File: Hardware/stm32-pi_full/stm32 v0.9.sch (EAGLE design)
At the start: 271 parts, among them J1 SOLDERJUMPERNO, Q1 MMBT3906, Q2 MMBT3904, Q3 MMBT3904, U1 ESP32-WROOM-32D, Y1 6MM_3.5MM_CRYSTAL

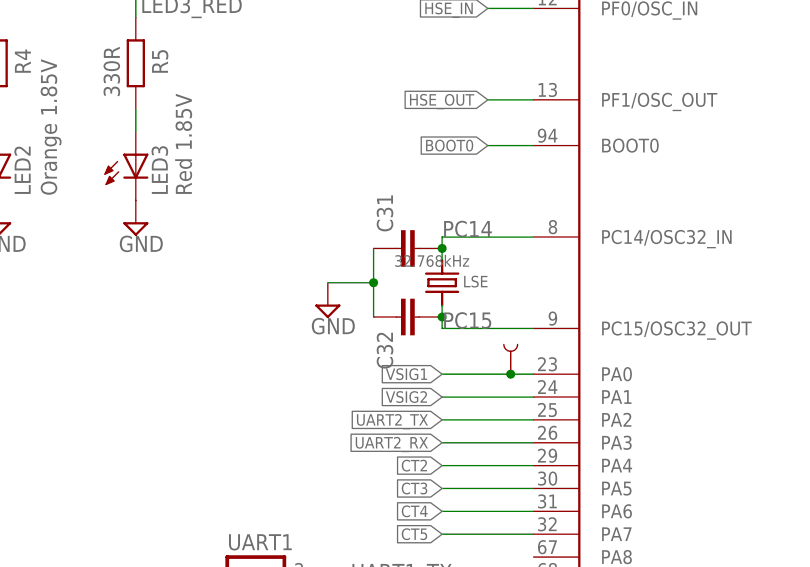
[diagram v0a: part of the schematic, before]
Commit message: non-Blocking UART transmissions
Saving 40ms at 460800 baud or 160ms at 115200 baud.
Now takes less than a millisecond to begin the UART transmit, happens in the background.
notes included on how to fire UART transmissions consequtively withing messing up the buffer or dropping transmissions.
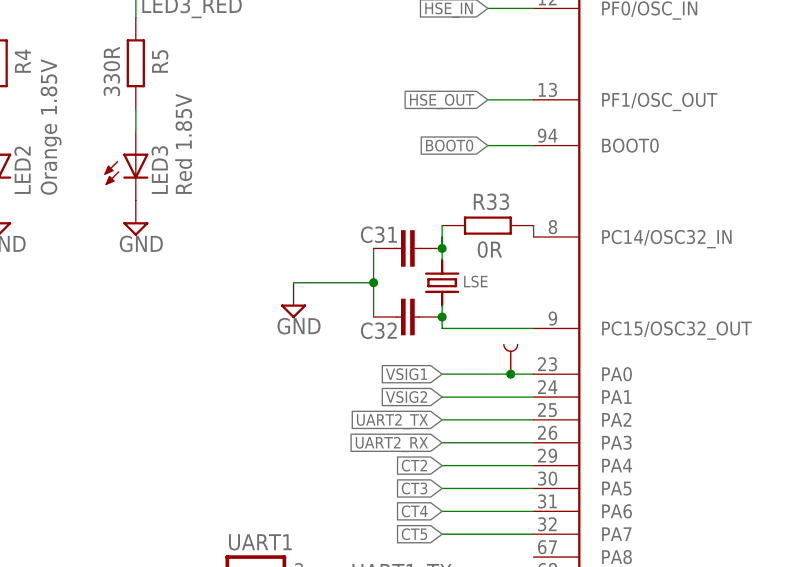
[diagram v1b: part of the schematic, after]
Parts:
- added R33: 0R, rcl:R-EU_R0603
- C29, C30: value 4.7nF -> 15pF
- C31, C32: value 2.2uF -> 10pF
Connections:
- new net N$1: R33.2, STM32F303VE.PC14/OSC32_IN
- net PC14: now also R33.1; no longer STM32F303VE.PC14/OSC32_IN
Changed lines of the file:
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@@
 <part name="R21" library="resistor" deviceset="R-EU_" device="R0603" value="0R"/>
 <part name="C21" library="rcl" library_urn="urn:adsk.eagle:library:334" deviceset="C-EU" device="C0805" package3d_urn="urn:adsk.eagle:package:23617/2" value="47uF"/>
-<part name="C29" library="rcl" library_urn="urn:adsk.eagle:library:334" deviceset="C-EU" device="C0603" package3d_urn="urn:adsk.eagle:package:23616/2" value="4.7nF"/>
-<part name="C30" library="rcl" library_urn="urn:adsk.eagle:library:334" deviceset="C-EU" device="C0603" package3d_urn="urn:adsk.eagle:package:23616/2" value="4.7nF"/>
+<part name="C29" library="rcl" library_urn="urn:adsk.eagle:library:334" deviceset="C-EU" device="C0603" package3d_urn="urn:adsk.eagle:package:23616/2" value="15pF"/>
+<part name="C30" library="rcl" library_urn="urn:adsk.eagle:library:334" deviceset="C-EU" device="C0603" package3d_urn="urn:adsk.eagle:package:23616/2" value="15pF"/>
 <part name="SUPPLY11" library="supply2" library_urn="urn:adsk.eagle:library:372" deviceset="GND" device=""/>
-<part name="C31" library="rcl" library_urn="urn:adsk.eagle:library:334" deviceset="C-EU" device="C0805" package3d_urn="urn:adsk.eagle:package:23617/2" value="2.2uF"/>
-<part name="C32" library="rcl" library_urn="urn:adsk.eagle:library:334" deviceset="C-EU" device="C0805" package3d_urn="urn:adsk.eagle:package:23617/2" value="2.2uF"/>
+<part name="C31" library="rcl" library_urn="urn:adsk.eagle:library:334" deviceset="C-EU" device="C0805" package3d_urn="urn:adsk.eagle:package:23617/2" value="10pF"/>
+<part name="C32" library="rcl" library_urn="urn:adsk.eagle:library:334" deviceset="C-EU" device="C0805" package3d_urn="urn:adsk.eagle:package:23617/2" value="10pF"/>
 <part name="SUPPLY27" library="supply2" library_urn="urn:adsk.eagle:library:372" deviceset="GND" device=""/>
 <part name="JP1" library="SparkFun-Jumpers" library_urn="urn:adsk.eagle:library:528" deviceset="JUMPER-SMT_3_1-NC_TRACE" device="_NO-SILK" package3d_urn="urn:adsk.eagle:package:39287/1"/>
@@
 <part name="R31" library="resistor" deviceset="R-EU_" device="R0603" value="0R"/>
 <part name="R32" library="resistor" deviceset="R-EU_" device="R0603" value="0R"/>
+<part name="R33" library="rcl" library_urn="urn:adsk.eagle:library:334" deviceset="R-EU_" device="R0603" package3d_urn="urn:adsk.eagle:package:23555/3" value="0R"/>
 </parts>
 <sheets>
@@
 <instance part="LSE" gate="G$1" x="53.34" y="15.24" smashed="yes" rot="R270">
 <attribute name="NAME" x="55.626" y="14.732" size="1.27" layer="95"/>
-<attribute name="VALUE" x="48.006" y="17.018" size="1.27" layer="96"/>
 </instance>
 <instance part="SUPPLY19" gate="GND" x="132.207" y="-206.629" smashed="yes">
@@
 </instance>
 <instance part="C31" gate="G$1" x="50.8" y="19.05" smashed="yes" rot="R270">
-<attribute name="NAME" x="46.101" y="25.146" size="1.778" layer="95" rot="R270"/>
+<attribute name="NAME" x="48.514" y="21.463" size="1.778" layer="95" rot="R180"/>
 </instance>
 <instance part="C32" gate="G$1" x="50.8" y="11.43" smashed="yes" rot="R270">
-<attribute name="NAME" x="46.101" y="9.906" size="1.778" layer="95" rot="R270"/>
+<attribute name="NAME" x="48.514" y="10.795" size="1.778" layer="95" rot="R180"/>
 </instance>
-<instance part="SUPPLY27" gate="GND" x="40.64" y="12.7" smashed="yes">
-<attribute name="VALUE" x="38.735" y="9.525" size="1.778" layer="96"/>
+<instance part="SUPPLY27" gate="GND" x="36.83" y="12.7" smashed="yes">
+<attribute name="VALUE" x="34.925" y="9.525" size="1.778" layer="96"/>
 </instance>
 <instance part="JP1" gate="G$1" x="177.8" y="71.628" smashed="yes" rot="R90"/>
@@
 <attribute name="NAME" x="237.49" y="263.1186" size="1.778" layer="95"/>
 </instance>
+<instance part="R33" gate="G$1" x="58.42" y="21.59" smashed="yes">
+<attribute name="NAME" x="56.642" y="23.3426" size="1.778" layer="95"/>
+<attribute name="VALUE" x="57.15" y="18.034" size="1.778" layer="96"/>
+</instance>
 </instances>
 <busses>
@@
 <wire x1="45.72" y1="15.24" x2="45.72" y2="19.05" width="0.1524" layer="91"/>
 <junction x="45.72" y="15.24"/>
-<wire x1="45.72" y1="15.24" x2="40.64" y2="15.24" width="0.1524" layer="91"/>
+<wire x1="45.72" y1="15.24" x2="36.83" y2="15.24" width="0.1524" layer="91"/>
 <pinref part="SUPPLY27" gate="GND" pin="GND"/>
 </segment>
@@
 <net name="PC14" class="0">
 <segment>
-<wire x1="53.34" y1="20.32" x2="63.5" y2="20.32" width="0.1524" layer="91"/>
-<pinref part="STM32F303VE" gate="G$1" pin="PC14/OSC32_IN"/>
-<label x="53.34" y="20.32" size="1.778" layer="95"/>
 <pinref part="LSE" gate="G$1" pin="1"/>
 <wire x1="53.34" y1="20.32" x2="53.34" y2="19.05" width="0.1524" layer="91"/>
@@
 <wire x1="53.34" y1="19.05" x2="53.34" y2="17.78" width="0.1524" layer="91"/>
 <junction x="53.34" y="19.05"/>
+<pinref part="R33" gate="G$1" pin="1"/>
+<wire x1="53.34" y1="21.59" x2="53.34" y2="19.05" width="0.1524" layer="91"/>
 </segment>
 </net>
@@
 <wire x1="53.34" y1="10.16" x2="63.5" y2="10.16" width="0.1524" layer="91"/>
 <pinref part="STM32F303VE" gate="G$1" pin="PC15/OSC32_OUT"/>
-<label x="53.34" y="10.16" size="1.778" layer="95"/>
 <pinref part="LSE" gate="G$1" pin="2"/>
 <wire x1="53.34" y1="10.16" x2="53.34" y2="11.43" width="0.1524" layer="91"/>
@@
 </segment>
 </net>
+<net name="N$1" class="0">
+<segment>
+<pinref part="STM32F303VE" gate="G$1" pin="PC14/OSC32_IN"/>
+<pinref part="R33" gate="G$1" pin="2"/>
+<wire x1="63.5" y1="20.32" x2="63.5" y2="21.59" width="0.1524" layer="91"/>
+</segment>
+</net>

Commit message: minor, uipdate BoMs
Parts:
- R21: value 0R -> 2k
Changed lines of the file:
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@@
 <part name="R13" library="resistor" deviceset="R-EU_" device="R0603" value="10k"/>
 <part name="R20" library="resistor" deviceset="R-EU_" device="R0603" value="10k"/>
-<part name="R21" library="resistor" deviceset="R-EU_" device="R0603" value="0R"/>
+<part name="R21" library="resistor" deviceset="R-EU_" device="R0603" value="2k"/>
 <part name="C21" library="rcl" library_urn="urn:adsk.eagle:library:334" deviceset="C-EU" device="C0805" package3d_urn="urn:adsk.eagle:package:23617/2" value="47uF"/>
 <part name="C29" library="rcl" library_urn="urn:adsk.eagle:library:334" deviceset="C-EU" device="C0603" package3d_urn="urn:adsk.eagle:package:23616/2" value="15pF"/>

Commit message: minor changes, some checks on proto v0.8 done.
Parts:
- removed Q4: (no value), microbuilder:MOSFET-P
- added C20, C34: 100nF, rcl:C-EUC0603
- added D36, D37: ESD5Z3.3T1G, microbuilder:DIODESOD-523
- R34, R35, R36: value (none) -> 0R
- R8: value 1.5k -> 100k
- renumbered JP4 to R34, JP5 to R35, JP6 to R36
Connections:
- new net N$19: D37.C, R8.1
- net +3V3: no longer Q4.D
- net +5V: now also D36.A
- net GND: now also C20.2; no longer Q4.G
- net N$16: now also D36.C, D37.A; no longer Q4.S, R8.1
- net NRST_STM: now also C34.1, C34.2
- net VBAT: now also C20.1

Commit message: Various checks.
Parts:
- added C35, C36: 2.2uF, rcl:C-EUC0805
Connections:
- net BIAS: now also C35.1, C36.1
- net GND: now also C35.2, C36.2
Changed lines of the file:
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@@
 <part name="RFM69HCW" library="rfm12b _ rfm69cw" deviceset="RFM12_SMD" device="SMD"/>
 <part name="SUPPLY33" library="supply2" library_urn="urn:adsk.eagle:library:372" deviceset="GND" device=""/>
-<part name="U$2" library="BOOST MODULE CN6009" deviceset="BOOST_MODULE" device=""/>
+<part name="U$2" library="BOOST MODULE CN6009" deviceset="BOOST_MODULE" device="" value="BOOST_MODULE"/>
 <part name="RB9_" library="rcl" library_urn="urn:adsk.eagle:library:334" deviceset="R-EU_" device="0207/7" package3d_urn="urn:adsk.eagle:package:23493/2" value="100R 0.1%"/>
 <part name="RB8_" library="rcl" library_urn="urn:adsk.eagle:library:334" deviceset="R-EU_" device="0207/7" package3d_urn="urn:adsk.eagle:package:23493/2" value="22r"/>
@@
 <part name="C20" library="rcl" library_urn="urn:adsk.eagle:library:334" deviceset="C-EU" device="C0603" package3d_urn="urn:adsk.eagle:package:23616/2" value="100nF"/>
 <part name="C34" library="rcl" library_urn="urn:adsk.eagle:library:334" deviceset="C-EU" device="C0603" package3d_urn="urn:adsk.eagle:package:23616/2" value="100nF"/>
+<part name="C35" library="rcl" library_urn="urn:adsk.eagle:library:334" deviceset="C-EU" device="C0805" package3d_urn="urn:adsk.eagle:package:23617/2" value="2.2uF"/>
+<part name="C36" library="rcl" library_urn="urn:adsk.eagle:library:334" deviceset="C-EU" device="C0805" package3d_urn="urn:adsk.eagle:package:23617/2" value="2.2uF"/>
+<part name="SUPPLY52" library="supply2" library_urn="urn:adsk.eagle:library:372" deviceset="GND" device=""/>
 </parts>
 <sheets>
@@
 <attribute name="NAME" x="37.719" y="110.744" size="1.778" layer="95" rot="R90"/>
 <attribute name="VALUE" x="42.799" y="110.744" size="1.778" layer="96" rot="R90"/>
+</instance>
+<instance part="C35" gate="G$1" x="163.83" y="109.22" smashed="yes">
+<attribute name="NAME" x="165.354" y="109.601" size="1.778" layer="95"/>
+<attribute name="VALUE" x="165.354" y="104.521" size="1.778" layer="96"/>
+</instance>
+<instance part="C36" gate="G$1" x="173.99" y="109.22" smashed="yes">
+<attribute name="NAME" x="175.514" y="109.601" size="1.778" layer="95"/>
+<attribute name="VALUE" x="175.514" y="104.521" size="1.778" layer="96"/>
+</instance>
+<instance part="SUPPLY52" gate="GND" x="170.18" y="99.06" smashed="yes">
+<attribute name="VALUE" x="168.275" y="95.885" size="1.778" layer="96"/>
 </instance>
 </instances>
@@
 <label x="-55.88" y="-20.32" size="1.778" layer="95" xref="yes"/>
 </segment>
+<segment>
+<pinref part="C35" gate="G$1" pin="2"/>
+<pinref part="C36" gate="G$1" pin="2"/>
+<wire x1="163.83" y1="104.14" x2="170.18" y2="104.14" width="0.1524" layer="91"/>
+<wire x1="170.18" y1="104.14" x2="173.99" y2="104.14" width="0.1524" layer="91"/>
+<wire x1="170.18" y1="104.14" x2="170.18" y2="101.6" width="0.1524" layer="91"/>
+<junction x="170.18" y="104.14"/>
+<pinref part="SUPPLY52" gate="GND" pin="GND"/>
+</segment>
 </net>
 <net name="+5V" class="1">
@@
 <junction x="137.16" y="86.36"/>
 </segment>
+<segment>
+<pinref part="C36" gate="G$1" pin="1"/>
+<pinref part="C35" gate="G$1" pin="1"/>
+<wire x1="173.99" y1="111.76" x2="170.18" y2="111.76" width="0.1524" layer="91"/>
+<wire x1="170.18" y1="111.76" x2="163.83" y2="111.76" width="0.1524" layer="91"/>
+<wire x1="170.18" y1="111.76" x2="170.18" y2="116.84" width="0.1524" layer="91"/>
+<junction x="170.18" y="111.76"/>
+<label x="170.18" y="116.84" size="1.778" layer="95" xref="yes"/>
+</segment>
 </net>
 <net name="N$2" class="0">
@@
 <wire x1="-76.2" y1="-236.22" x2="-256.54" y2="-236.22" width="0.254" layer="91"/>
 <wire x1="-256.54" y1="-236.22" x2="-256.54" y2="-68.58" width="0.254" layer="91"/>
-<wire x1="-256.54" y1="144.78" x2="-256.54" y2="228.6" width="0.254" layer="91"/>
-<wire x1="-256.54" y1="228.6" x2="-76.2" y2="228.6" width="0.254" layer="91"/>
+<wire x1="-256.54" y1="144.78" x2="-256.54" y2="228.6" width="0.1524" layer="91"/>
+<wire x1="-256.54" y1="228.6" x2="-76.2" y2="228.6" width="0.1524" layer="91"/>
 <wire x1="193.04" y1="-137.16" x2="431.8" y2="-137.16" width="0.254" layer="91"/>
 <wire x1="109.22" y1="144.78" x2="109.22" y2="205.74" width="0.254" layer="91"/>

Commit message: v0.9 backup
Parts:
- removed C50*: 2.2uF, rcl:C-EUC0805
- removed D22, D23: ESD5Z3.3T1G, microbuilder:DIODESOD-523
- removed GOLD_ORB_SM1: OSHWLOGOLOGO8MM, oshw:OSHWLOGOLOGO8MM
- removed JP2, JP3, JP7, JP8: JUMPER-SMT_3_1-NC_TRACE_SILK, SparkFun-Jumpers:JUMPER-SMT_3_1-NC_TRACE_SILK
- removed Q11_, Q12_, Q13_, Q14_, Q15_, Q16_, Q17_, Q18_, Q19_, Q21, Q22, Q33: (no value), adafruit:MOSFET-NREFLOW
- removed R29: 10K, rcl:R-EU_R0603
- removed RB1: 22r 0.3W 1%, rcl:R-EU_R1210
- removed RB1Q, RB2, RB2Q, RB3, RB3Q, RB4, RB4Q, RB5, RB5Q, RB6, RB6Q, RB7, RB7Q, RB8, RB8Q: 22r, rcl:R-EU_R1210
- removed RB9: 100R 0.1%, rcl:R-EU_R1210
- removed RB9Q: 22R 0.1%, rcl:R-EU_R1210
- removed SJ2: SOLDERJUMPERNO, SparkFun:SOLDERJUMPERNO
- removed ST_LINK: 455-1750-1-ND, SparkFun-Connectors:CONN_03
- removed TP1, TP11, TP12, TP13, TP14, TP15, TP16, TP2, TP21, TP3: TEST-POINT3, SparkFun-Connectors:TEST-POINT3
- removed TP17, TP6: TEST-POINTPOGO_PTH, SparkFun-Connectors:TEST-POINTPOGO_PTH
- added C37, C38, C48: 100nF, resistor:C-EUC0603
- added C39, C43, C44: 22uF, rcl:C-EUC0805
- added C49: 10pF, rcl:C-EUC0805
- added C50: (no value), rcl:C-EUC0603
- added CANBUS: TX/RX, con-lstb-db:MA02-1
- added FB2: (no value), microbuilder:FERRITE
- added FB3, FB4, FB5, FB6, FB7, FB8, FB9: (no value), microbuilder:FERRITE_0603
- added JP10, JP11, JP12, JP13, JP14, JP15, JP16, JP17, JP18: JUMPER-SMT_2_NO_NO-SILK_ROUND, SparkFun-Jumpers:JUMPER-SMT_2_NO_NO-SILK_ROUND
- added JP19: JUMPER-SMT_3_NO_NO-SILK, SparkFun-Jumpers:JUMPER-SMT_3_NO_NO-SILK
- added JP4: JUMPER-SMT_2_NC_TRACE_NO-SILK, SparkFun-Jumpers:JUMPER-SMT_2_NC_TRACE_NO-SILK
- added JP5, JP6, JP9: 0R, rcl:R-EU_R0603
- added MCP1825(ANALOG): MCP1825SOT-223-3, SteelCaveRobotics-Power:MCP1825SOT-223-3
- added R37: 0R, resistor:R-EU_R0603
- added R38: 1k, resistor:R-EU_R0603
- added RB1A, RB1B: 22r 0.3W 1%, rcl:R-EU_R0805
- added RB2A, RB2B, RB3A, RB3B, RB4A, RB4B, RB5A, RB5B, RB6A, RB6B, RB7A, RB7B, RB8A, RB8B: 22r, rcl:R-EU_R0805
- added RB9A, RB9B: 100R 0.1%, rcl:R-EU_R0805
- added SV3: (no value), con-lstb-db:MA03-1
- BOOT_STM, UART1: device SparkFun:M02PTH -> con-lstb-db:MA02-1
- C11, C14, C18: value 2.2uF -> 22uF
- C12, C21, C33: value 47uF -> 22uF
- C13, C20: value 100nF -> 2.2uF
- C17, C3, C4: value 2.2uF -> 100nF; device rcl:C-EUC0805 -> resistor:C-EUC0603
- C23: value 2.2uF -> 1uf; device rcl:C-EUC0805 -> rcl:C-EUC0603
- C34: device rcl:C-EUC0603 -> resistor:C-EUC0603
- C35, C36: value 2.2uF -> 1uF; device rcl:C-EUC0805 -> rcl:C-EUC0603
- C9: value 100nF -> 1uF; device resistor:C-EUC0603 -> rcl:C-EUC0603
- CT1, CT2, CT3, CT4, CT5, CT6, CT7, CT8, CT9: device IotaWatt_parts:STEREO_SMD -> sj-3523-smt:SJ-3523-SMTSJ-352X-SMT_SERIES-1313220
- FB1: MPN (none) -> MH1608-601Y
- JP1: value JUMPER-SMT_3_1-NC_TRACE_NO-SILK -> JUMPER-SMT_2_NC_TRACE_NO-SILK; device SparkFun-Jumpers:JUMPER-SMT_3_1-NC_TRACE_NO-SILK -> SparkFun-Jumpers:JUMPER-SMT_2_NC_TRACE_NO-SILK
- PS1: MPN REF193GSZ -> REF196GSZ
- Q1: value MMBT3906 -> (none); device Transistor:MMBT3906 -> microbuilder:TRANSISTOR_PNPSOT23-REFLOW; MPN (none) -> SMMBT3906LT1G
- Q2, Q3: value MMBT3904 -> (none); device Transistor:MMBT3904 -> microbuilder:TRANSISTOR_NPN; MPN (none) -> KST3904MTF
- R25, R26, R27: value 10k -> 9k1
- R30: value 0R -> 1k5; device resistor:R-EU_R0603 -> rcl:R-EU_R0603
- R31, R32: value 0R -> 20R; device resistor:R-EU_R0603 -> rcl:R-EU_R0603
- R33: value 0R -> 10k
- R41, R42, R43: value 120k -> 100k
- RB1_, RB2_, RB3_, RB4_, RB5_, RB6_, RB7_, RB8_, RB9_: device rcl:R-EU_0207/7 -> rcl:R-EU_0207/10
- TP4: value TPB1,27 -> TEST-POINTPOGO_PTH; device testpad:TPB1,27 -> SparkFun-Connectors:TEST-POINTPOGO_PTH
- renumbered TERM2 to TB2
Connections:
- net BIAS* renamed BIAS_
- net BOOT0 renamed BOOT_STM
- net LED2_YELLOW renamed LED2
- net LED3_RED renamed LED3
- removed net AC1_MOS: Q21.S, R25.1, R30.2, R43.1, R53.1, SJ37.1
- removed net AC2_MOS: Q22.S, R26.1, R31.2, R42.1, R52.1, SJ36.1
- removed net AC3_MOS: Q33.S, R27.1, R32.2, R41.2, R51.1, SJ35.1
- removed net ESP_PWR: R29.2, STM32F303VE.PC11
- removed net LED1_GREEN: R3.2, STM32F303VE.PD8
- removed net MOS1: Q11_.G, STM32F303VE.PE7, TP17.1
- removed net MOS2: Q12_.G, STM32F303VE.PE8
- removed net MOS3: Q13_.G, STM32F303VE.PE9
- removed net MOS4: Q14_.G, STM32F303VE.PE10
- removed net MOS5: Q15_.G, STM32F303VE.PE11
- removed net MOS6: Q16_.G, STM32F303VE.PE12
- removed net MOS7: Q17_.G, STM32F303VE.PE13
- removed net MOS8: Q18_.G, STM32F303VE.PE14
- removed net MOS9: Q19_.G, STM32F303VE.PE15
- removed net N$12: JP1.2, R22.2
- removed net N$37: Q14_.D, RB4Q.2
- removed net N$38: CT6.2, D24.A, D8.C, Q16_.S, RB6.1, RB6_.1, RF6.1
- removed net N$39: CT5.2, D20.A, D9.C, Q15_.S, RB5.1, RB5_.1, RF5.1
- removed net N$40: CT4.2, D10.C, D25.A, Q14_.S, RB4.1, RB4_.1, RF4.1
- removed net N$45: Q19_.D, RB9Q.2
- removed net N$46: Q18_.D, RB8Q.2
- removed net N$47: Q15_.D, RB5Q.2
- removed net N$48: Q16_.D, RB6Q.2
- removed net N$49: Q17_.D, RB7Q.2
- removed net N$7: FB1.P$1, USB-C.VBUS1, USB-C.VBUS2
- removed net SD_CLK: JP8.2, U$7.CLK
- removed net SD_CS_: JP2.2, U$7.CD/DAT3
- removed net SD_MISO: JP7.2, U$7.DAT0
- removed net SD_MOSI: JP3.2, U$7.CMD
- removed net SPI4_CS_SDCARD_MASTER: JP2.1, STM32F303VE.PE3, TP13.1
- removed net VMOS1: Q21.G, STM32F303VE.PC0, TP6.1
- removed net VMOS2: Q22.G, STM32F303VE.PC1
- removed net VMOS3: Q33.G, STM32F303VE.PC2
- new net +3V3ANA: C43.1, D1.C, D15.C, D16.C, D19.C, D20.C, D24.C, D25.C, D27.C, D28.C, D29.C, D30.C, D31.C, D32.C, JP19.1, MCP1825(ANALOG).+3V3, TERM3.P$5, TP7.1
- new net +5V_A: C39.1, FB8.P$1, MCP1825(ANALOG).IN
- new net +5V_D: C21.1, FB9.P$1, MCP1825.IN
- new net +5V_REF: C11.1, C37.1, FB6.P$1, PS1.!SHDN, PS1.VIN
- new net +5V_USB: C34.1, D40*1.C, FB1.P$1, USB-C.VBUS1, USB-C.VBUS2
- new net AC1_: JP9.2, R25.1, R43.1, R53.1, SJ37.1
- new net AC2_: JP6.2, R26.1, R42.1, R52.1, SJ36.1
- new net AC3_: JP5.2, R27.1, R41.2, R51.1, SJ35.1
- new net AGND: C11.2, C13.2, C17.2, C23.2, C35.2, C36.2, C37.2, C38.2, C39.2, C43.2, C50.1, CF1.1, CF2.1, CF3.1, CF4.1, CF5.1, CF6.1, CF7.1, CF8.1, CF9.1, CV1.2, CV2.2, CV3.2, D10.A, D11.A, D12.A, D13.A, D14.A, D2.A, D3.A, D4.A, D5.A, D6.A, D7.A, D8.A, D9.A, EXPANSION.1, EXPANSION.2, FB3.P$2, MCP1825(ANALOG).GND@2, PS1.GND, R23.1, R38.2, STM32F303VE.VSSA/VREF-, TERM3.P$6
- new net CAN_RX: CANBUS.1, STM32F303VE.PD0
- new net CAN_TX: CANBUS.2, STM32F303VE.PD1
- new net CT_IN4: CT4.2, D10.C, D25.A, RB4A.1, RB4B.1, RB4_.1, RF4.1
- new net CT_IN5: CT5.2, D20.A, D9.C, RB5A.1, RB5B.1, RB5_.1, RF5.1
- new net CT_IN6: CT6.2, D24.A, D8.C, RB6A.1, RB6B.1, RB6_.1, RF6.1
- new net CT_IN7: CT7.2, D19.A, D7.C, RB7A.1, RB7B.1, RB7_.1, RF7.1
- new net CT_IN8: CT8.2, D16.A, D6.C, RB8A.1, RB8B.1, RB8_.1, RF8.1
- new net CT_IN9: CT9.2, D15.A, D5.C, RB9A.1, RB9B.1, RB9_.1, RF9.1
- new net DGND: BOOT_ESP.1, C1.2, C10.2, C18.2, C19.2, C21.2, C22.2, C24.2, C25.2, C26.2, C27.2, C28.2, C29.2, C3.2, C30.2, C31.2, C32.2, C33.2, C40.2, C41.2, C42.2, C45.2, C46.2, C47.2, C49.2, C5.2, C6.2, C7.2, C8.2, D17.A, D18.A, D26.A, D33.A, D35.A, EXPANSION.14, EXPANSION.25, EXPANSION.9, FB4.P$2, G1.-, LED1.C, LED2.C, LED3.C, LED4.C, MCP1825.GND@2, OLED.4, PCB2.GND@14, PCB2.GND@20, PCB2.GND@25, PCB2.GND@30, PCB2.GND@34, PCB2.GND@39, PCB2.GND@6, PCB2.GND@9, Q2.E, Q3.E, R14.1, R15.1, R16.1, R2.2, RJ1.1, RJ1.3, RJ1.5, RJ2.1, RJ2.3, RJ2.5, S2.1, STM32F303VE.PF4, STM32F303VE.VSS@2, STM32F303VE.VSS@3, STM32F303VE.VSS@4, SV1.1, SV2.1, TB2.P$3, TERM1.P$6, U$2.GND, U$2.GND., U$7.GND, U$7.VSS, U1.GND, U1.IO19, UART_STM.1
- new net GND_USB: C34.2, D40*1.A, FB2.P$1, USB-C.GND1, USB-C.GND2, USB-C.SHIELD
- new net LED1: R3.2, STM32F303VE.PC8
- new net N$13: CT3.4, JP14.2
- new net N$22: CT8.4, JP17.2
- new net NRST_STM_: C9.2, STM32F303VE.NRST
- new net OPAMP_INVERT-: C20.2, R37.2, R38.1, STM32F303VE.PD8
- new net RGND: C14.2, C2.2, C44.2, C48.2, FB7.P$2, J$1.GND@0, J$1.GND@1, J$1.GND@2, J$1.GND@3, RFM69HCW.GND, RFM69HCW.GND@1
- new net SD_CARD_STM: JP1.2, STM32F303VE.PD7
- new net SD_CS: JP1.1, U$7.CD/DAT3, U1.IO35
- new net USB_DM: R32.2, STM32F303VE.PA11
- new net USB_DM_: R32.1, USB-C.D1-
- new net USB_DP: R30.1, R31.2, STM32F303VE.PA12
- new net USB_DP_: R31.1, USB-C.D1+
- new net USB_RST: R30.2, STM32F303VE.PD3
- new net VDD: C14.1, C2.1, C44.1, FB5.P$1, RFM69HCW.VDD
- new net VDDA: C13.1, C17.1, JP19.2, STM32F303VE.VDDA
- net +3V3: now also C3.1, C5.1, C6.1, C8.1, FB5.P$2, R13.2, R20.2, R33.1, S1.P; no longer C13.1, C14.1, C17.1, C2.1, C4.2, C5.2, C6.2, C8.2, C9.2, D1.C, D15.C, D16.C, D19.C, D20.C, D22.C, D23.C, D24.C, D25.C, D27.C, D28.C, D29.C, D30.C, D31.C, D32.C, JP1.1, R13.1, R20.1, RFM69HCW.VDD, SJ2.2, STM32F303VE.VDDA, TERM3.P$5
- net +5V: now also C12.1, C15.1, C4.1, FB6.P$2, FB8.P$2, FB9.P$2, TP4.1; no longer C11.1, C12.2, C15.2, C21.1, C3.1, D40*1.C, MCP1825.IN, PS1.VIN, TP4.TP
- net AC1: no longer Q21.D
- net AC2: no longer Q22.D
- net AC3: no longer Q33.D
- net ANT: now also C48.1
- net BIAS: now also C20.1, JP11.1, JP13.1, JP15.1, JP16.1, JP17.1, JP18.1, R37.1, RB4A.2, RB4B.2, RB5A.2, RB5B.2, RB6A.2, RB6B.2, RB7A.2, RB7B.2, RB8A.2, RB8B.2, RB9A.2, RB9B.2; no longer CT4.4, CT5.4, CT6.4, CT7.4, CT8.4, CT9.4, RB4.2, RB4Q.1, RB5.2, RB5Q.1, RB6.2, RB6Q.1, RB7.2, RB7Q.1, RB8.2, RB8Q.1, RB9.2, RB9Q.1
- net BIAS_IN: now also C50.2; no longer C50*.2
- net CT1: now also STM32F303VE.PB0; no longer STM32F303VE.PC3
- net CT2: now also STM32F303VE.PB1; no longer STM32F303VE.PA4
- net CT3: now also STM32F303VE.PE7; no longer STM32F303VE.PA5
- net CT4: now also STM32F303VE.PE8; no longer STM32F303VE.PA6
- net CT5: now also STM32F303VE.PE9; no longer STM32F303VE.PA7
- net CT6: now also STM32F303VE.PE10; no longer STM32F303VE.PC4
- net CT7: now also STM32F303VE.PE11; no longer STM32F303VE.PC5
- net CT8: now also STM32F303VE.PE12; no longer STM32F303VE.PB2
- net CT9: now also STM32F303VE.PE13; no longer STM32F303VE.PB11
- net CT_IN1: now also RB1A.1, RB1B.1; no longer Q11_.S, RB1.1
- net CT_IN2: now also RB2A.1, RB2B.1; no longer Q12_.S, RB2.1
- net CT_IN3: now also RB3A.1, RB3B.1; no longer Q13_.S, RB3.1
- net ESP_PWR_PRE: no longer R29.1
- net GND: now also C12.2, C15.2, C4.2, FB2.P$2, FB3.P$1, FB4.P$1, FB7.P$1; no longer BOOT_ESP.1, C1.2, C10.2, C11.2, C12.1, C13.2, C14.2, C15.1, C17.2, C18.2, C19.2, C2.2, C20.2, C21.2, C22.2, C23.2, C24.2, C25.2, C26.2, C27.2, C28.2, C29.2, C3.2, C30.2, C31.2, C32.2, C33.2, C35.2, C36.2, C4.1, C40.2, C41.2, C42.2, C45.2, C46.2, C47.2, C5.1, C50*.1, C6.1, C7.2, C8.1, C9.1, CF1.1, CF2.1, CF3.1, CF4.1, CF5.1, CF6.1, CF7.1, CF8.1, CF9.1, CV1.2, CV2.2, CV3.2, D10.A, D11.A, D12.A, D13.A, D14.A, D17.A, D18.A, D2.A, D22.A, D23.A, D26.A, D3.A, D33.A, D35.A, D4.A, D40*1.A, D5.A, D6.A, D7.A, D8.A, D9.A, EXPANSION.1, EXPANSION.14, EXPANSION.2, EXPANSION.25, EXPANSION.9, G1.-, J$1.GND@0, J$1.GND@1, J$1.GND@2, J$1.GND@3, LED1.C, LED2.C, LED3.C, LED4.C, MCP1825.GND@2, OLED.4, PCB2.GND@14, PCB2.GND@20, PCB2.GND@25, PCB2.GND@30, PCB2.GND@34, PCB2.GND@39, PCB2.GND@6, PCB2.GND@9, PS1.GND, Q2.E, Q3.E, R14.1, R15.1, R16.1, R2.2, R23.1, RFM69HCW.GND, RFM69HCW.GND@1, RJ1.1, RJ1.3, RJ1.5, RJ2.1, RJ2.3, RJ2.5, S1.P, S2.1, STM32F303VE.VSS@2, STM32F303VE.VSS@3, STM32F303VE.VSS@4, STM32F303VE.VSSA/VREF-, SV1.1, SV2.1, TB2.P$3, TERM1.P$6, TERM3.P$6, U$2.GND, U$2.GND., U$7.GND, U$7.VSS, U1.GND, U1.IO19, UART_STM.1, USB-C.GND1, USB-C.GND2, USB-C.SHIELD
- net HSPI_CLK: no longer JP8.3
- net HSPI_CS0: no longer JP2.3
- net HSPI_ID/MOSI: no longer JP3.3
- net HSPI_Q/MISO: no longer JP7.3
- net N$1: now also CT1.4, JP10.2; no longer R33.2, STM32F303VE.PC14/OSC32_IN
- net N$10: now also CT5.4, JP13.2; no longer CT7.2, D19.A, D7.C, Q17_.S, RB7.1, RB7_.1, RF7.1
- net N$2: now also CT4.4, JP11.2; no longer CT9.2, D15.A, D5.C, Q19_.S, RB9.1, RB9_.1, RF9.1
- net N$20: now also CT6.4, JP15.2; no longer Q11_.D, RB1Q.2
- net N$21: now also CT9.4, JP16.2; no longer Q12_.D, RB2Q.2
- net N$23: now also CT7.4, JP18.2; no longer Q13_.D, RB3Q.2
- net N$26: now also JP10.1, RB1A.2, RB1B.2; no longer CT1.4, RB1.2, RB1Q.1
- net N$27: now also JP12.1, RB2A.2, RB2B.2; no longer CT2.4, RB2.2, RB2Q.1
- net N$28: now also JP14.1, RB3A.2, RB3B.2; no longer CT3.4, RB3.2, RB3Q.1
- net N$8: now also CT2.4, JP12.2; no longer CT8.2, D16.A, D6.C, Q18_.S, RB8.1, RB8_.1, RF8.1
- net NRST_STM: now also C9.1, R33.2, SV3.3; no longer C34.1, C34.2, STM32F303VE.NRST, ST_LINK.3
- net PC14: now also STM32F303VE.PC14/OSC32_IN; no longer R33.1
- net PULSE1_RJ45: now also JP4.1; no longer STM32F303VE.PA12
- net PULSE_2_RJ45: now also C49.1
- net RPI_GPIO16: now also STM32F303VE.PD4; no longer STM32F303VE.PD12
- net RPI_GPIO20: now also STM32F303VE.PD5; no longer STM32F303VE.PD13
- net RPI_PWR: no longer TP11.1
- net SCL: now also R20.1, STM32F303VE.PA8; no longer R13.2, STM32F303VE.PC8
- net SDA: now also R13.1; no longer R20.2
- net SPI1_CLK_SLAVE: now also U$7.CLK; no longer TP1.1
- net SPI1_MISO_SLAVE: now also U$7.DAT0; no longer TP2.1
- net SPI1_MOSI_SLAVE: now also U$7.CMD; no longer TP3.1
- net SPI1_NSS_SLAVE: no longer TP21.1
- net SPI4_CLK_MASTER: no longer JP8.1, TP12.1
- net SPI4_CS_RFM69_MASTER: now also STM32F303VE.PE3; no longer STM32F303VE.PE4, TP14.1
- net SPI4_MISO_MASTER: no longer JP7.1, TP15.1
- net SPI4_MOSI_MASTER: no longer JP3.1, TP16.1
- net SWCLK: now also SV3.1; no longer ST_LINK.1
- net SWDIO: now also JP4.2, SV3.2; no longer ST_LINK.2
- net VBAT: no longer C20.1
- net VREF+: now also C38.1, JP19.3, R22.2; no longer JP1.3, SJ2.1, TP7.1
- net VSIG1: now also D32.A, JP9.1; no longer D30.A, R30.1
- net VSIG2: now also JP6.1; no longer R31.1
- net VSIG3: now also D30.A, JP5.1; no longer D32.A, R32.1
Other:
- note added: "2.2uF was also okay in previous testing."
- note added: "BIAS IN"
- note added: "BIAS OUT"
- note added: "FEEDBACK"
- note added: "I2C protection"
- note added: "I2C pullups"
- note added: "STAR GND"
- note added: "Schematic Version v0.9"
- note added: "USB Input"
- note added: "VDDA TESTING"
- note added: "check transistor part numbers"
- note added: "gpio - literally"
- note added: "maybe DNGA comes off the ana supply with FB in series"
- note added: "mbus etc."
- note added: "supperfluous?"
- note removed: "1"
- note removed: "2"
- note removed: "4"
- note removed: "BIAS"
- note removed: "BOOT_STM"
- note removed: "Frequency 8MHZ to 32MHZ 25pF max."
- note removed: "USB"
- note removed: "VREG Datasheet suggests 1uF Output Capacitor"
- note removed: "i2c pullups"
- moved on the sheet: BOOT_STM, C12, C13, C15, C17, C20, C21, C23, C29, C3, C30, C33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
